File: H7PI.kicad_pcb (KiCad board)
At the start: 4 copper layers, 65 x 30 mm, 49 parts, among them J1 XKTF-015-N, J2 Header_2x10, J3 microUSB, J4 AFC07-S24ECA-00, J5 Header_2x20, J6 microUSB, J7 Header_1x2, J8 Header_1x1, J9 Header_1x1, Q1 CJ2101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

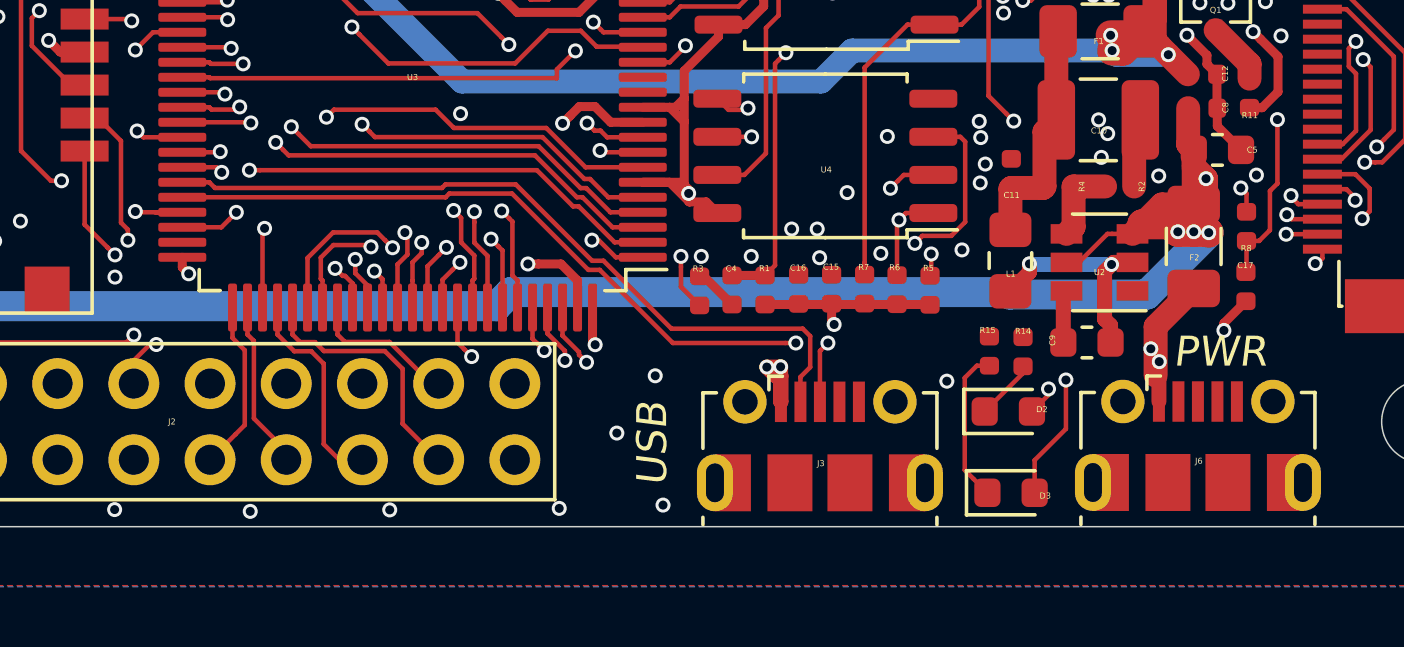
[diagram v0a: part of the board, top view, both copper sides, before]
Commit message: v0.3 1. 增加电压支持到12V 2. 增加双USB口通信（不能同时用） 3. 增加USB通孔，用于底板扩展，正常为DNP状态
Signed-off-by: fuhua-chen <fuhua-chen@outlook.com>
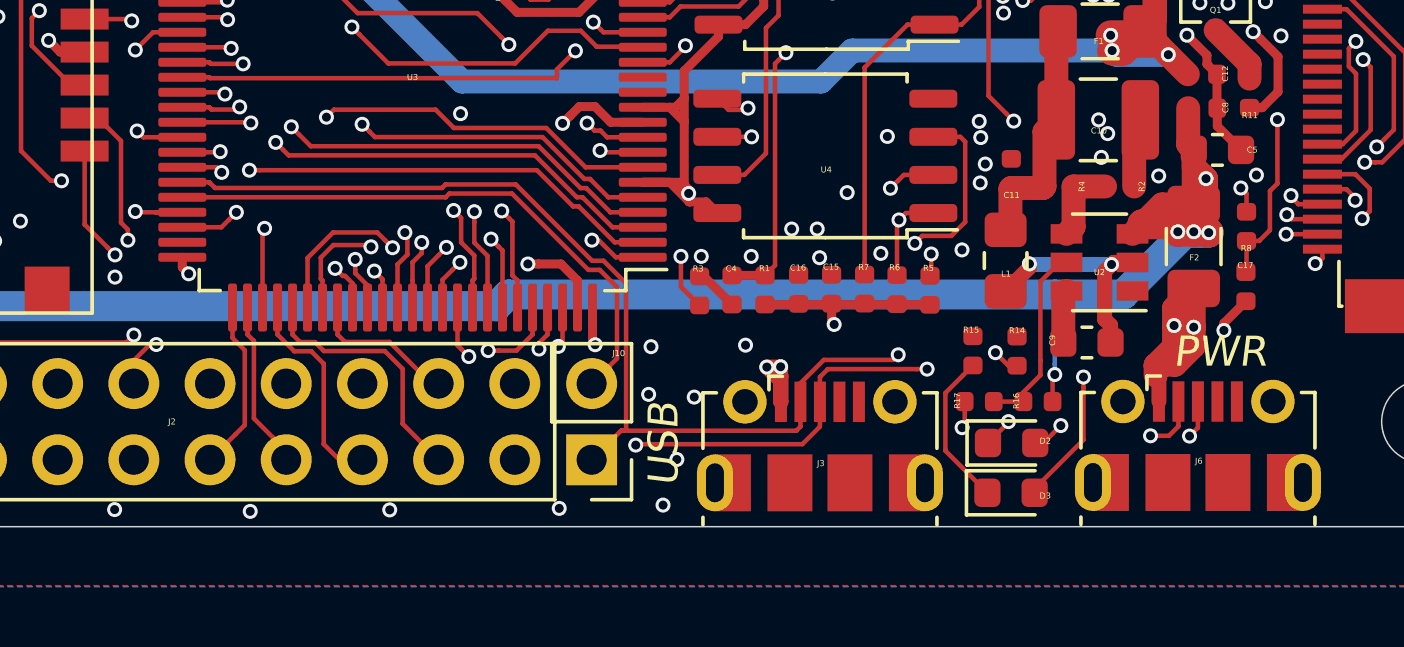
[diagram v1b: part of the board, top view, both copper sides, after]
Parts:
- added J10: DNP, PinHeader_1x02_P2.54mm_Vertical, F.Cu at (163.8, 87.8)
- added R16: 100k, R_0402_1005Metric, F.Cu at (178.7, 85.8)
- added R17: 33k, R_0402_1005Metric, F.Cu at (176.7, 85.8)
- moved D2 1.06 mm to (177.8, 87.2)
- moved R15 0.55 mm to (176.5, 84.1)
- moved R14 0.20 mm to (178.0, 84.2)
- moved L1 0.16 mm to (177.6, 81.1)
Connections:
- J3 pad 4: Net-(J3-Pad4) -> (no net)
- J6 pad 2: Net-(J6-Pad2) -> /USB_N
- J6 pad 3: Net-(J6-Pad3) -> /USB_P
- J6 pad 4: Net-(J6-Pad4) -> (no net)
- U2 pad 5: /VBUS -> Net-(R16-Pad2)
- U3 pad 12: Net-(U3-Pad12) -> (no net)
- U3 pad 13: Net-(U3-Pad13) -> (no net)
- U5 pad 3: Net-(U5-Pad3) -> (no net)
- U5 pad 7: Net-(U5-Pad7) -> (no net)
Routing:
- net /USB_N: track 25.5 -> 45.3 mm, vias 0 -> 2
- net /USB_P: track 25.7 -> 45.1 mm, vias 2 -> 3
- net Net-(R16-Pad2): track 0.00 -> 6.36 mm
- net Net-(F2-Pad2): track 20.6 -> 26.8 mm
- net Net-(D2-Pad1): track 2.03 -> 4.37 mm, vias 0 -> 2
- net /IO16: track 26.9 -> 24.9 mm
- net Net-(D2-Pad2): track 23.5 -> 25.1 mm
- net /IO14: track 20.3 -> 19.0 mm
- net /VBUS: track 103.6 -> 104.6 mm, vias 4 -> 5
- net GND: track 29.8 -> 30.7 mm, vias 91 -> 94
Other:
- board text added: "H7PI ZERO V0.3 20191228"
- board text removed: "H7PI ZERO V0.2 20190924"
